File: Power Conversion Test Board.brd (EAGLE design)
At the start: 136.7 x 125.3 mm, 46 parts, among them U1 LM2678, U2 LM2678

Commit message: Routed board
board is routed
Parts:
- moved C5 41.6 mm to (30.5, 100.6), turned to 0 degrees
- moved C4 40.5 mm to (30.5, 85.9), turned to 0 degrees
- moved C1 39.5 mm to (30.5, 97.3), turned to 0 degrees
- moved C3 38.7 mm to (30.5, 89.7), turned to 0 degrees
- moved C2 38.3 mm to (30.5, 93.4), turned to 0 degrees
- moved C10 29.4 mm to (63.1, 97.3)
- moved C11 29.0 mm to (63.1, 93.5)
- moved C12 29.0 mm to (63.1, 89.7)
- moved C13 29.0 mm to (63.1, 85.9)
- moved R1 22.4 mm to (62.6, 82.4)
- moved J1 14.4 mm to (5.44, 71.2)
- moved R3 13.3 mm to (72.7, 81.6)
- moved C27 12.9 mm to (72.8, 85.9)
- moved C26 12.9 mm to (72.8, 89.7)
- moved C25 12.8 mm to (72.8, 93.5)
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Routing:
- net 12VGND: track 0.00 -> 194.6 mm, vias 0 -> 1
- net 5VGND: track 9.21 -> 197.6 mm, vias 0 -> 5
- net +12V: track 0.00 -> 152.2 mm, vias 0 -> 6
- net +5V_3.3V: track 0.00 -> 136.2 mm, vias 0 -> 4
- net 3.3VGND: track 0.00 -> 59.3 mm
- net +5V: track 0.00 -> 51.3 mm, vias 0 -> 2
- net N$7: track 0.00 -> 50.8 mm, vias 0 -> 2
- net N$1: track 0.00 -> 37.6 mm, vias 0 -> 3
- net N$8: track 4.68 -> 34.2 mm, vias 0 -> 2
- net N$4: track 4.81 -> 24.2 mm, vias 0 -> 1
- net N$10: track 0.00 -> 8.81 mm
- net +3.3V: track 0.00 -> 7.12 mm
- net N$2: track 0.00 -> 4.76 mm
- net N$3: track 0.00 -> 3.80 mm
- added copper zone on layer 1, net +12V
- added copper zone on layer 1, net 12VGND
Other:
- board text added: "+12V"
- board text added: "12V GND"
- board text added: "3.3V GND"
- board text added: "5V GND"

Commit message: ripped board up and started over
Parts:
- removed C13: .01uF, Seeed-Capacitor:AVX-A
- removed C5: 470nF, SparkFun-Capacitors:0402
- removed C8, C9: 150uf, Seeed-Capacitor:AVX-A
- added C14, C29, C30, C31: 10uF, PowerComponents:CTAN(7.30_4.30MM)
- added J5, J6: (no value), SparkFun-Connectors:BANANA_CONN
- C1, C15, C16, C17, C18: device SparkFun-Capacitors:1206 -> PowerComponents:CTAN(7.30_4.30MM)
- C10, C24: value 100uF -> 150uF; device Seeed-Capacitor:AVX-A -> PowerComponents:CTAN(7.30_4.30MM)
- C11, C25: value 10uF -> 150uF; device Seeed-Capacitor:AVX-A -> PowerComponents:CTAN(7.30_4.30MM)
- C12, C26: value .1uF -> 150uF; device Seeed-Capacitor:AVX-A -> PowerComponents:CTAN(7.30_4.30MM)
- C19: value 470nF -> 100uF; device SparkFun-Capacitors:0402 -> PowerComponents:CTAN(7.30_4.30MM)
- C2: value 10uF -> .1uF; device SparkFun-Capacitors:1206 -> PowerComponents:CTAN(7.30_4.30MM)
- C21: value 150uf -> 10uF; device Seeed-Capacitor:AVX-A -> PowerComponents:CTAN(7.30_4.30MM)
- C22: value 150uf -> .1uF; device Seeed-Capacitor:AVX-A -> PowerComponents:CTAN(7.30_4.30MM)
- C23: value 150uf -> .01uF; device Seeed-Capacitor:AVX-A -> PowerComponents:CTAN(7.30_4.30MM)
- C27: value .01uF -> 100uF; device Seeed-Capacitor:AVX-A -> PowerComponents:CTAN(7.30_4.30MM)
- C3: value 10uF -> 0.47uF; device SparkFun-Capacitors:1206 -> rcl:C0603
- C4: value 10uF -> .01uF; device SparkFun-Capacitors:1206 -> PowerComponents:CTAN(7.30_4.30MM)
- C7: value 150uf -> 0.47uF; device Seeed-Capacitor:AVX-A -> rcl:C0603
- moved C23 216.0 mm to (-104.4, 96.0), flipped to the top
- moved C21 216.0 mm to (-104.4, 84.3), flipped to the top
- moved C22 215.8 mm to (-104.4, 90.2), flipped to the top
- moved C18 201.3 mm to (-116.1, 78.5), flipped to the top
- moved C17 201.3 mm to (-116.1, 84.3), flipped to the top
- moved C16 201.3 mm to (-116.1, 90.2), flipped to the top
- moved C15 201.2 mm to (-116.1, 96.0), flipped to the top
- moved C19 178.1 mm to (-92.7, 78.5), flipped to the top
- moved C27 177.4 mm to (-104.4, 78.5), flipped to the top
- moved C7 168.8 mm to (-116.1, 73.9)
- moved R3 167.8 mm to (-95.0, 73.9), flipped to the top
- moved R1 167.0 mm to (-104.1, 73.9)
- moved C28 159.3 mm to (-86.9, 29.2), turned to 180 degrees
- moved R4 153.7 mm to (-88.6, 24.4)
- moved U$5 149.9 mm to (-149.9, 1.27)
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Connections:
- net +12V: now also C14.+, C15.+, C16.+, C17.+, C18.+, C29.+, C3.1, C30.+, C31.+, C7.1; no longer C1.2, C15.2, C16.2, C17.2, C18.2, C19.2, C2.2, C3.2, C4.2, C5.2
- net +3.3V: now also J5.P$1
- net +5V: now also C10.+, C11.+, C12.+, J6.P$1; no longer C7.+, C8.+, C9.+
- net +5V_3.3V: now also C24.+, C25.+, C26.+; no longer C21.+, C22.+, C23.+
- net 12VGND: now also C1.+, C14.-, C15.-, C16.-, C17.-, C18.-, C19.+, C2.+, C21.+, C22.+, C23.+, C29.-, C3.2, C30.-, C31.-, C4.+, C7.2; no longer C1.1, C10.+, C11.+, C12.+, C13.+, C15.1, C16.1, C17.1, C18.1, C19.1, C2.1, C24.+, C25.+, C26.+, C3.1, C4.1, C5.1
- net 3.3VGND: now also C1.-, C19.-, C2.-, C4.-, R3.2, R5.1, U$10.P$1, U$3.P$1, U$3.P$3, U2.4, U2.TAB
- net 5VGND: now also C21.-, C22.-, C23.-; no longer C10.-, C11.-, C12.-, C13.-, C24.-, C25.-, C26.-, R3.2, R5.1, U$10.P$1, U$3.P$1, U$3.P$3, U2.4, U2.TAB
- net N$4: now also C24.-, C25.-, C26.-; no longer C21.-, C22.-, C23.-
- net N$8: now also C10.-, C11.-, C12.-; no longer C7.-, C8.-, C9.-
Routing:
- net 12VGND: track 194.6 -> 0.00 mm, vias 1 -> 0
- net 5VGND: track 197.6 -> 4.65 mm, vias 5 -> 0
- net +12V: track 152.2 -> 0.00 mm, vias 6 -> 0
- net +5V_3.3V: track 136.2 -> 0.00 mm, vias 4 -> 0
- net 3.3VGND: track 59.3 -> 0.00 mm
- net +5V: track 51.3 -> 0.00 mm, vias 2 -> 0
- net N$7: track 50.8 -> 0.00 mm, vias 2 -> 0
- net N$1: track 37.6 -> 0.00 mm, vias 3 -> 0
- net N$8: track 34.2 -> 4.65 mm, vias 2 -> 0
- net N$4: track 24.2 -> 0.00 mm, vias 1 -> 0
- net N$10: track 8.81 -> 0.00 mm
- net +3.3V: track 7.12 -> 0.00 mm
- net N$2: track 4.76 -> 0.00 mm
- net N$3: track 3.80 -> 0.00 mm
- removed copper zone on layer 1, net +12V
- removed copper zone on layer 1, net 12VGND
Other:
- board text removed: "+12V"
- board text removed: "12V GND"
- board text removed: "3.3V GND"
- board text removed: "5V GND"

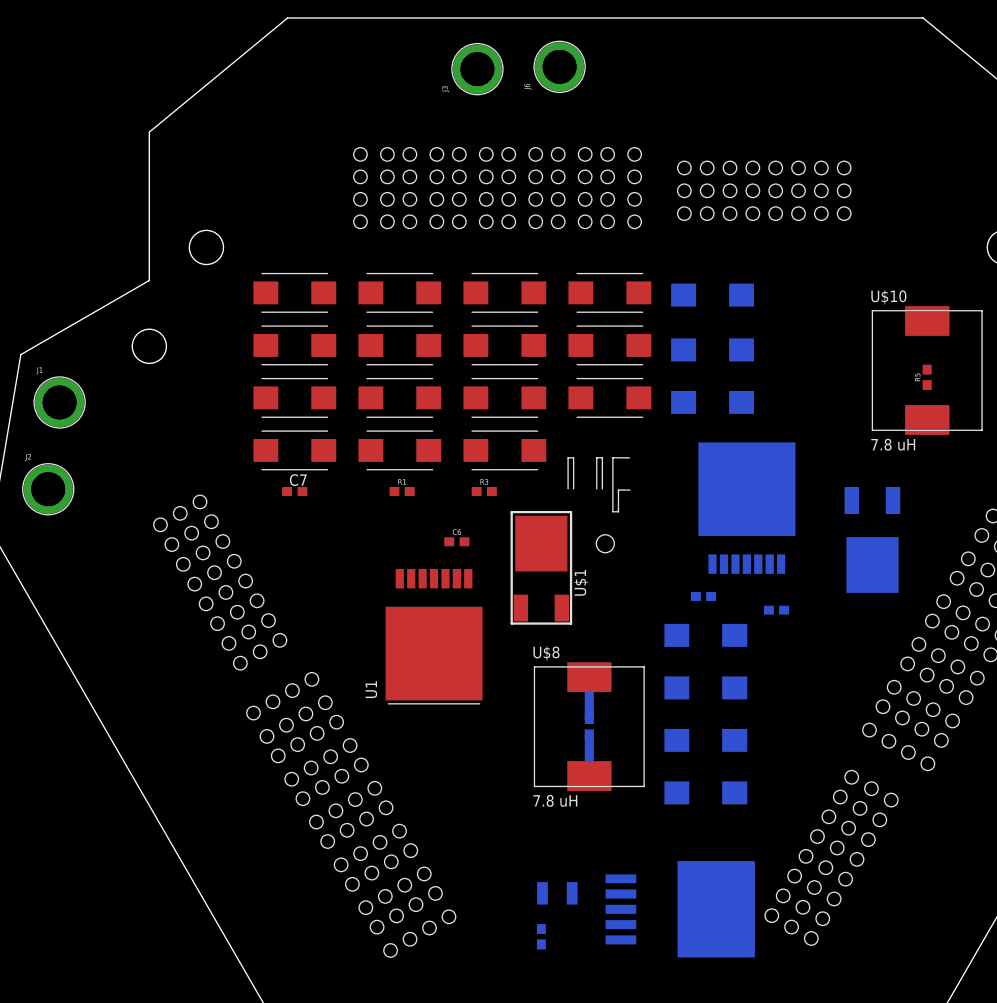
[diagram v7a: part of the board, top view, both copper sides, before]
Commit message: Updated board positioning
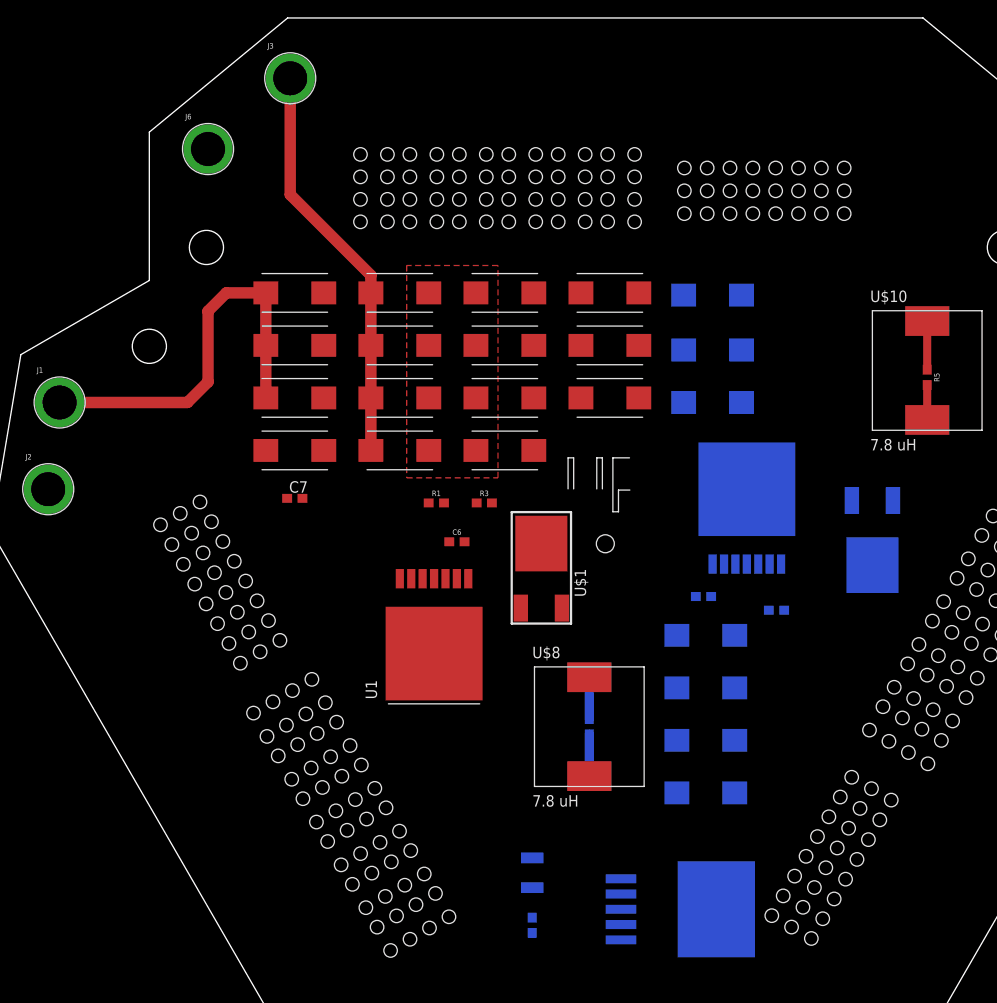
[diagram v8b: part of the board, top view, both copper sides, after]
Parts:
- moved J6 40.2 mm to (-125.7, 112.0), turned to 0 degrees
- moved J3 20.9 mm to (-116.6, 119.9), turned to 0 degrees
- moved C23 17.5 mm to (-104.4, 78.5), turned to 180 degrees
- moved C27 17.5 mm to (-104.4, 96.0), turned to 180 degrees
- moved C21 5.84 mm to (-104.4, 90.2), turned to 180 degrees
- moved C22 5.84 mm to (-104.4, 84.3), turned to 180 degrees
- moved R1 4.02 mm to (-100.3, 72.6)
- moved C28 3.61 mm to (-89.7, 31.5), turned to 90 degrees
- moved R4 1.63 mm to (-89.7, 25.7)
- moved R3 1.27 mm to (-95.0, 72.6)
- moved C7 0.76 mm to (-116.1, 73.2)
- turned R5 to 270 degrees
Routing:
- net 5VGND: track 4.65 -> 49.8 mm
- net +12V: track 0.00 -> 44.3 mm
- net 3.3VGND: track 0.00 -> 5.41 mm
- net N$4: track 0.00 -> 3.89 mm
- added copper zone on layer 1, net 12VGND
